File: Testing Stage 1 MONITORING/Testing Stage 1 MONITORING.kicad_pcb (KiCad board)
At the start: 2 copper layers, 61.1 x 70 mm, 80 parts, among them J1 Conn_01x06_Socket, J2 Conn_01x03_Pin, J3 Conn_01x02, Q1 PMOS, Q2 NMOS, Q5 NMOS, Q6 NMOS, SW1 SW_Push, U1 BQ76920PW, U2 BQ78350DBT, U3 BQ76200PW

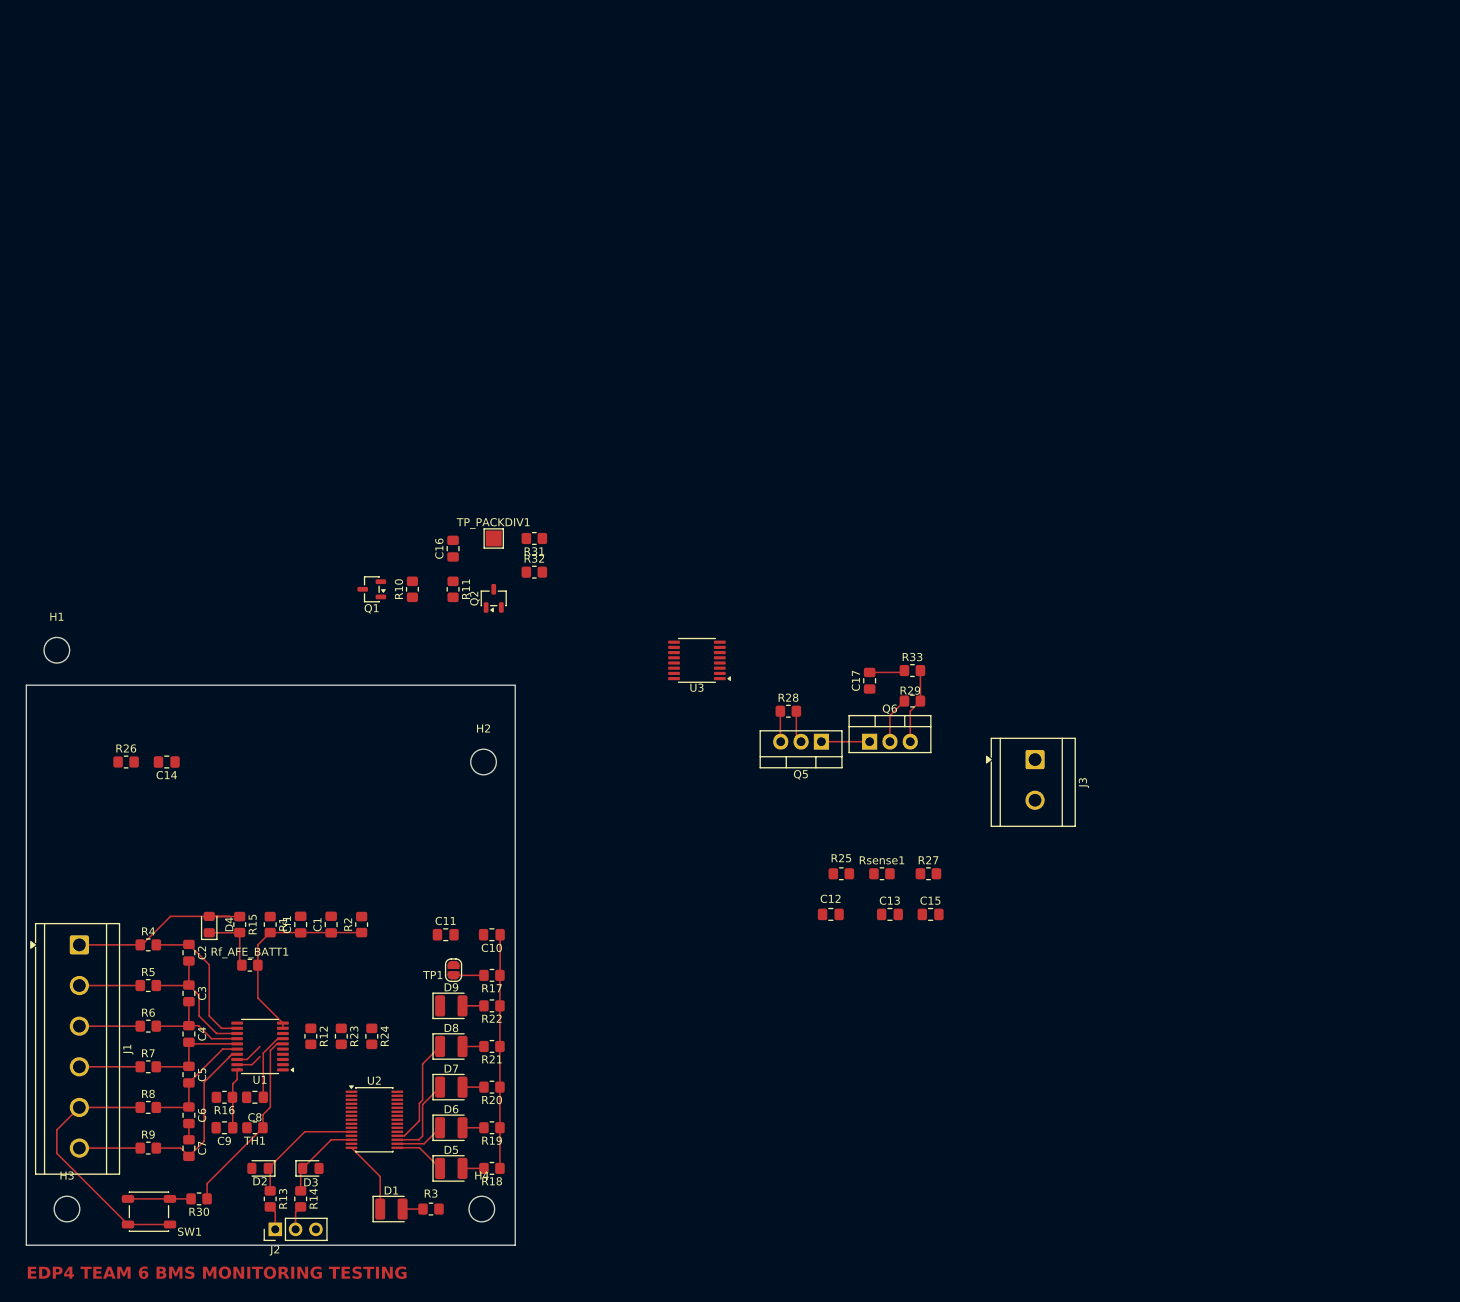
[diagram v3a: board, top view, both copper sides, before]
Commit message: updated layout and almost complete routing - need to address DRC
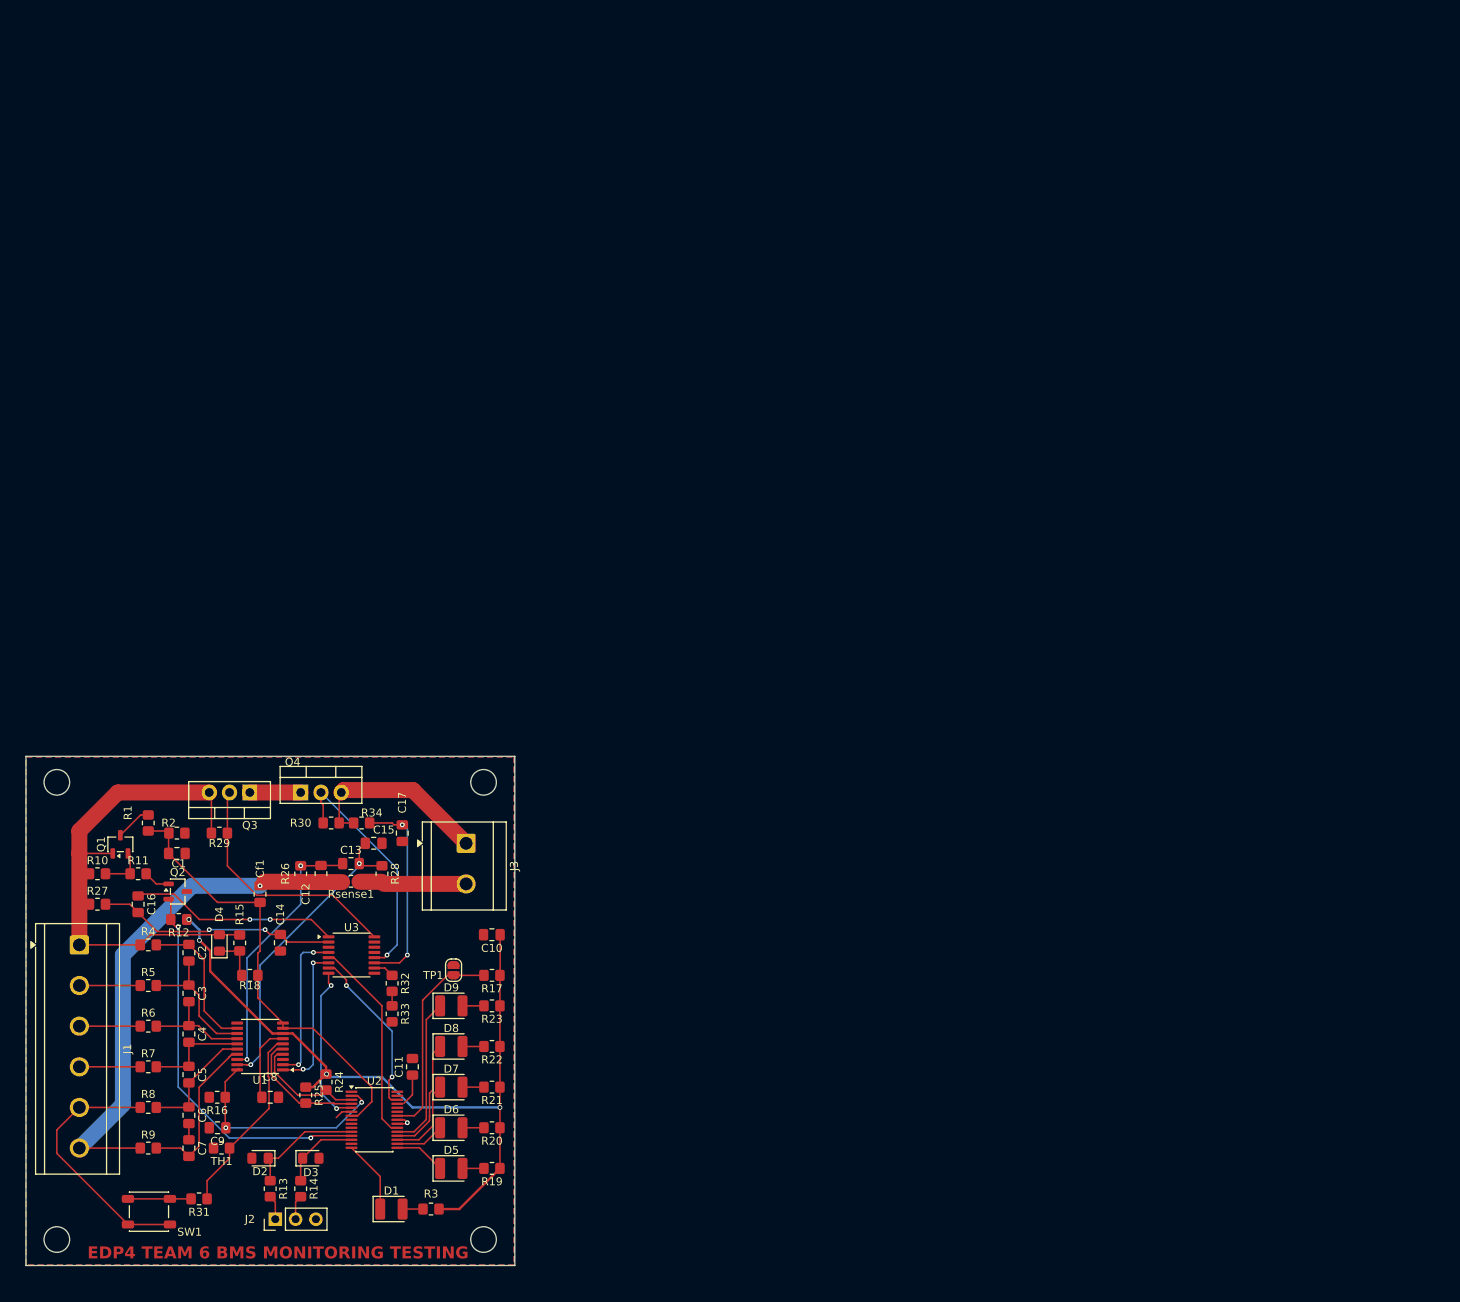
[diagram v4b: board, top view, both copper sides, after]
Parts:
- removed TP_PACKDIV1: TestPoint, TestPoint:TestPoint_Pad_2.0x2.0mm
- moved R30 74.2 mm to (73.7, 97.8)
- moved R29 72.7 mm to (59.7, 99.1)
- moved J3 71.9 mm to (90.5, 100.3)
- moved Q3 71.7 mm to (63.5, 94.0)
- moved R34 71.4 mm to (77.5, 97.8), turned to 180 degrees
- moved Q4 71.4 mm to (69.8, 94.0)
- moved C15 70.2 mm to (79.0, 100.3)
- moved R28 68.3 mm to (80.0, 104.1), turned to -90 degrees
- moved C13 67.7 mm to (76.1, 102.9)
- moved R26 67.6 mm to (69.8, 104.1), turned to -90 degrees
- moved Rsense1 66.4 mm to (76.1, 105.1)
- moved C12 63.9 mm to (72.4, 104.1), turned to -90 degrees
- moved C17 61.4 mm to (82.5, 99.1)
- moved C16 59.4 mm to (49.5, 108.0), turned to -90 degrees
- moved R32 58.4 mm to (81.3, 117.8), turned to -90 degrees
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- renumbered Q5 to Q3, Q6 to Q4, Rf_AFE_BATT1 to R18, R18 to R19, R19 to R20, R20 to R21, R21 to R22, R22 to R23, R23 to R24, R24 to R25, R25 to R26, R26 to R27, R27 to R28, R28 to R29, R29 to R30, R30 to R31, R31 to R32, R32 to R33, R33 to R34
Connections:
- net /HS_SW_PACKDIV renamed Net-(R32-Pad2)
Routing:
- net /VCC: track 29.2 -> 93.8 mm, vias 0 -> 4
- net GND: track 9.64 -> 72.5 mm, vias 0 -> 2
- net /VEN: track 0.00 -> 48.6 mm, vias 0 -> 2
- net /SRN: track 3.28 -> 38.7 mm, vias 0 -> 2
- net /Top_cell_stack: track 27.9 -> 62.4 mm
- net /BAT: track 25.3 -> 55.6 mm
- net /SRP: track 3.54 -> 33.6 mm, vias 0 -> 2
- net Net-(U3-BAT): track 0.00 -> 30.0 mm, vias 0 -> 2
- net /CHG_GATE: track 4.05 -> 31.3 mm
- net Net-(U3-VDDCP): track 0.00 -> 26.1 mm, vias 0 -> 2
- net /HS_SW_CP_EN: track 0.00 -> 25.7 mm
- net /DSG_GATE: track 5.83 -> 30.4 mm, vias 0 -> 1
- net Net-(U2-~{MRST}): track 3.80 -> 26.0 mm
- net Net-(U3-PACK): track 4.45 -> 25.7 mm, vias 0 -> 2
- net /HS_SW_PMON_EN: track 0.00 -> 21.2 mm, vias 0 -> 2
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- added copper zone on B.Cu, net GND
- added copper zone on F.Cu, net GND
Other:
- board size 61.1 x 70 mm -> 61.1 x 63.7 mm

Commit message: working layout and routing no DRC error - but ugly
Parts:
- moved C8 5.80 mm to (60.6, 134.0), turned to 180 degrees
- moved TH1 2.54 mm to (60.0, 141.0)
- moved C9 0.64 mm to (59.5, 136.5)
- moved R16 0.64 mm to (59.4, 131.4)
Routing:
- net GND: track 72.5 -> 101.8 mm, vias 2 -> 9
- net Net-(U1-CAP1): track 9.00 -> 12.7 mm
- net /Cell_one: track 32.3 -> 35.5 mm
- net /TS1_AFE: track 23.8 -> 26.2 mm
- net /VCC: track 93.8 -> 95.7 mm, vias 4 -> 5
- net /ALERT_AFE: track 28.7 -> 29.7 mm
- net /HS_SW_PMON_EN: track 21.2 -> 22.1 mm
- net /BAT: track 55.6 -> 55.1 mm

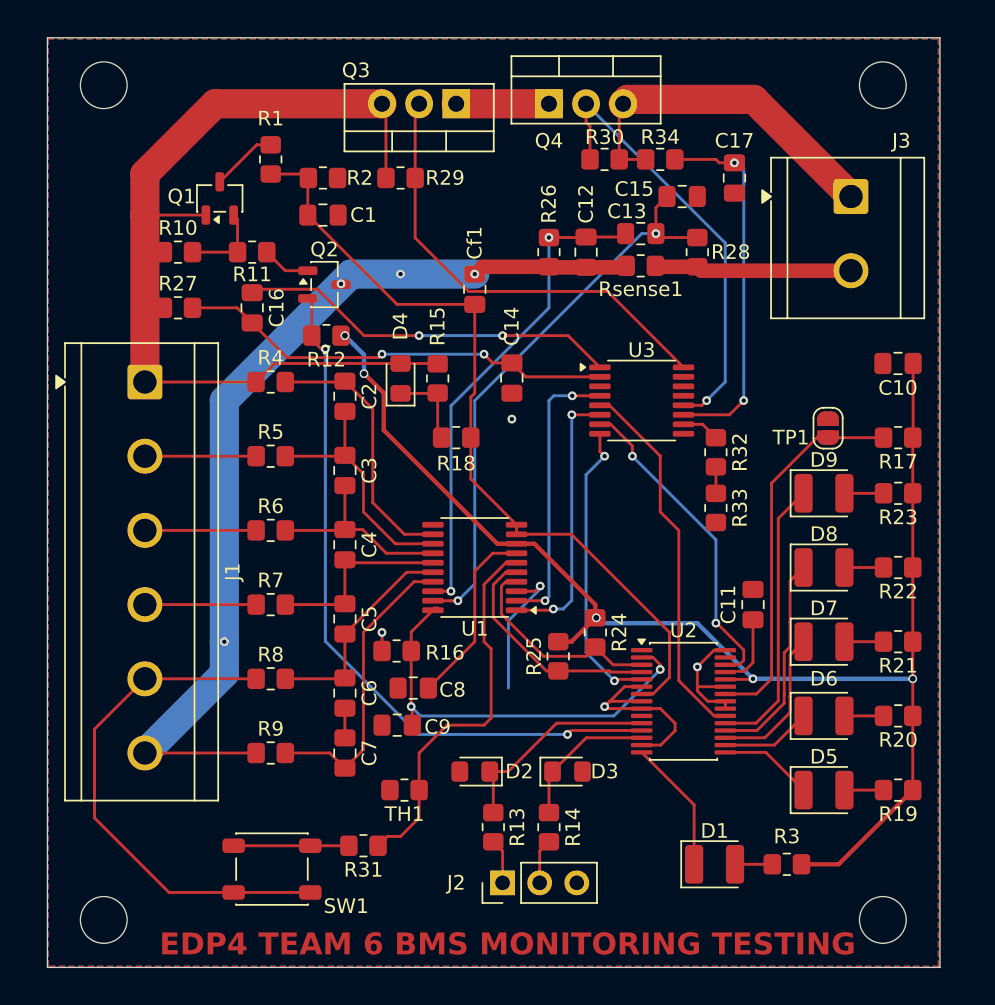
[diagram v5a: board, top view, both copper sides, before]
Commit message: refinements - moving battery pack off the PCB
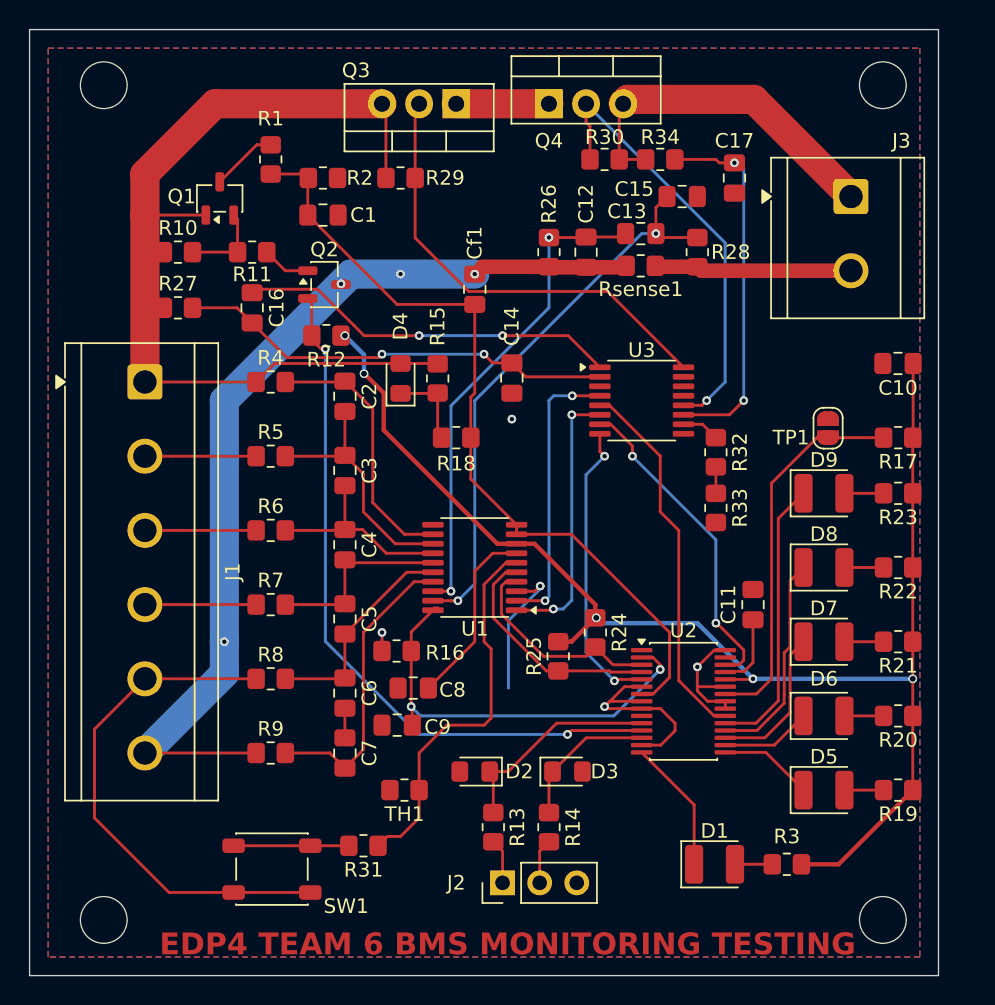
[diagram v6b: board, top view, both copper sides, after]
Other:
- board size 61.1 x 63.7 mm -> 62.2 x 64.8 mm
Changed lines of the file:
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@@
 	)
 	(gr_rect
-		(start 35.51 89.46)
-		(end 96.62 153.11)
+		(start 34.29 88.9)
+		(end 96.52 153.67)
 		(stroke
 			(width 0.05)
@@
 			)
 			(justify left bottom)
-		)
-	)
-	(dimension
-		(type orthogonal)
-		(layer "F.Cu")
-		(pts
-			(xy 96.52 89.535) (xy 96.62 153.11)
-		)
-		(height 11.938)
-		(orientation 1)
-		(format
-			(prefix "")
-			(suffix "")
-			(units 3)
-			(units_format 0)
-			(precision 4)
-			(suppress_zeroes yes)
-		)
-		(style
-			(thickness 0.2)
-			(arrow_length 1.27)
-			(text_position_mode 0)
-			(arrow_direction outward)
-			(extension_height 0.58642)
-			(extension_offset 0.5)
-			(keep_text_aligned yes)
-		)
-		(gr_text "63.575"
-			(at 106.658 121.3225 90)
-			(layer "F.Cu")
-			(effects
-				(font
-					(size 1.5 1.5)
-					(thickness 0.3)
-				)
-			)
-		)
-	)
-	(dimension
-		(type orthogonal)
-		(layer "F.Cu")
-		(pts
-			(xy 35.56 89.535) (xy 96.62 89.46)
-		)
-		(height -4.699)
-		(orientation 0)
-		(format
-			(prefix "")
-			(suffix "")
-			(units 3)
-			(units_format 0)
-			(precision 4)
-			(suppress_zeroes yes)
-		)
-		(style
-			(thickness 0.2)
-			(arrow_length 1.27)
-			(text_position_mode 0)
-			(arrow_direction outward)
-			(extension_height 0.58642)
-			(extension_offset 0.5)
-			(keep_text_aligned yes)
-		)
-		(gr_text "61.06"
-			(at 66.09 83.036 0)
-			(layer "F.Cu")
-			(effects
-				(font
-					(size 1.5 1.5)
-					(thickness 0.3)
-				)
-			)
 		)
 	)
@@
 		(polygon
 			(pts
-				(xy 35.56 89.535) (xy 96.52 89.535) (xy 96.52 153.035) (xy 35.56 153.035)
+				(xy 35.56 90.17) (xy 95.25 90.17) (xy 95.25 152.4) (xy 35.56 152.4)
 			)
 		)
